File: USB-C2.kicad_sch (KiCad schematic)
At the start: 92 parts, among them J4 USB_C_Receptacle, J5 I2C2_PD_Controller, J6 I2C_Mux, J7 I2C_EEPROM, SW2 FW_Upgrade, U10 24LC256, U11 TPD4E02B04DQA, U12 TPD4E02B04DQA, U13 TPD4E02B04DQA, U14 TUSB1142IRNQR_C5216209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

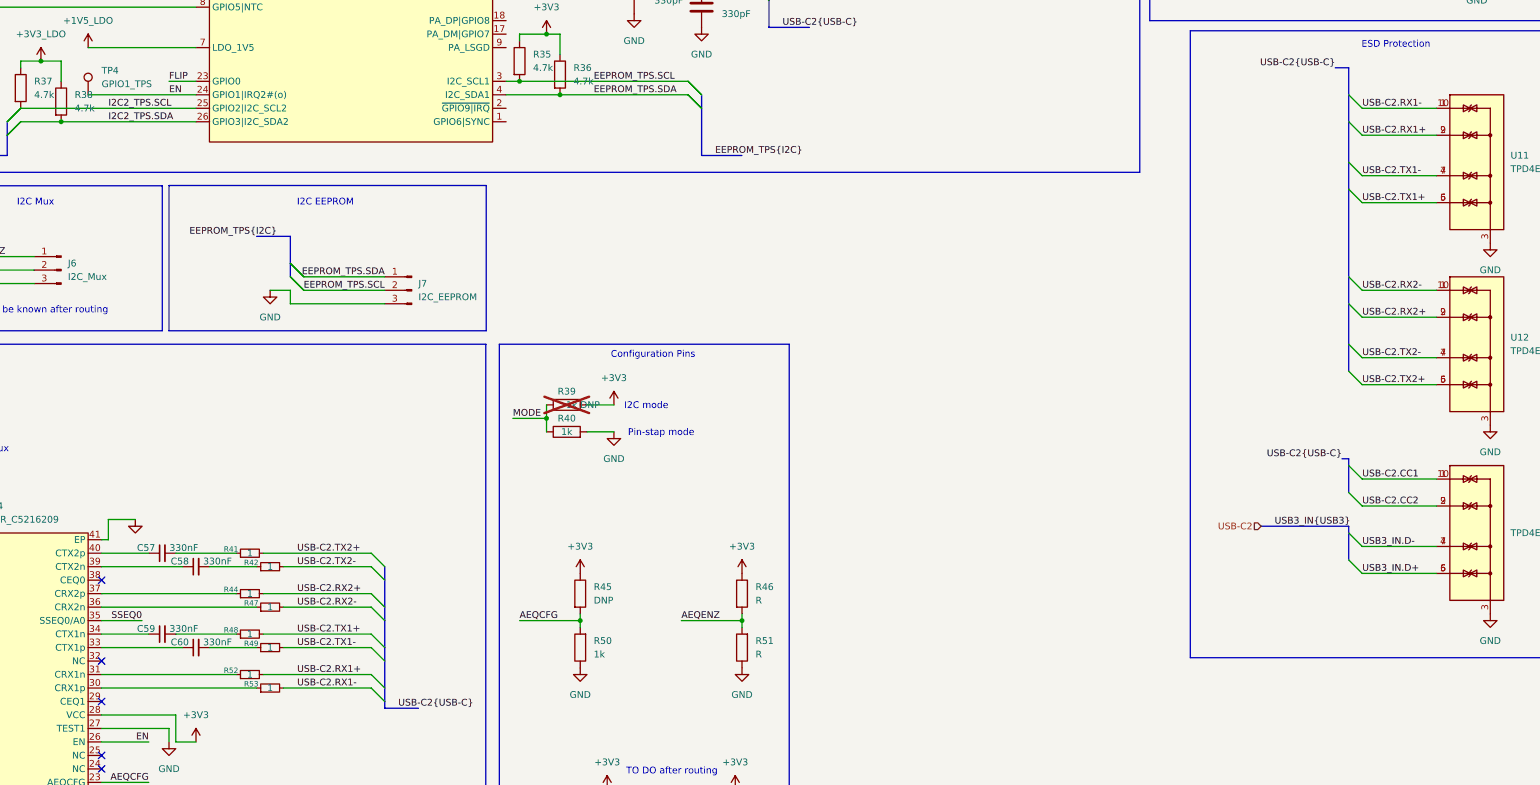
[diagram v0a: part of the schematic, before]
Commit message: Next net class label fixes, swap of the SS lines for better routing
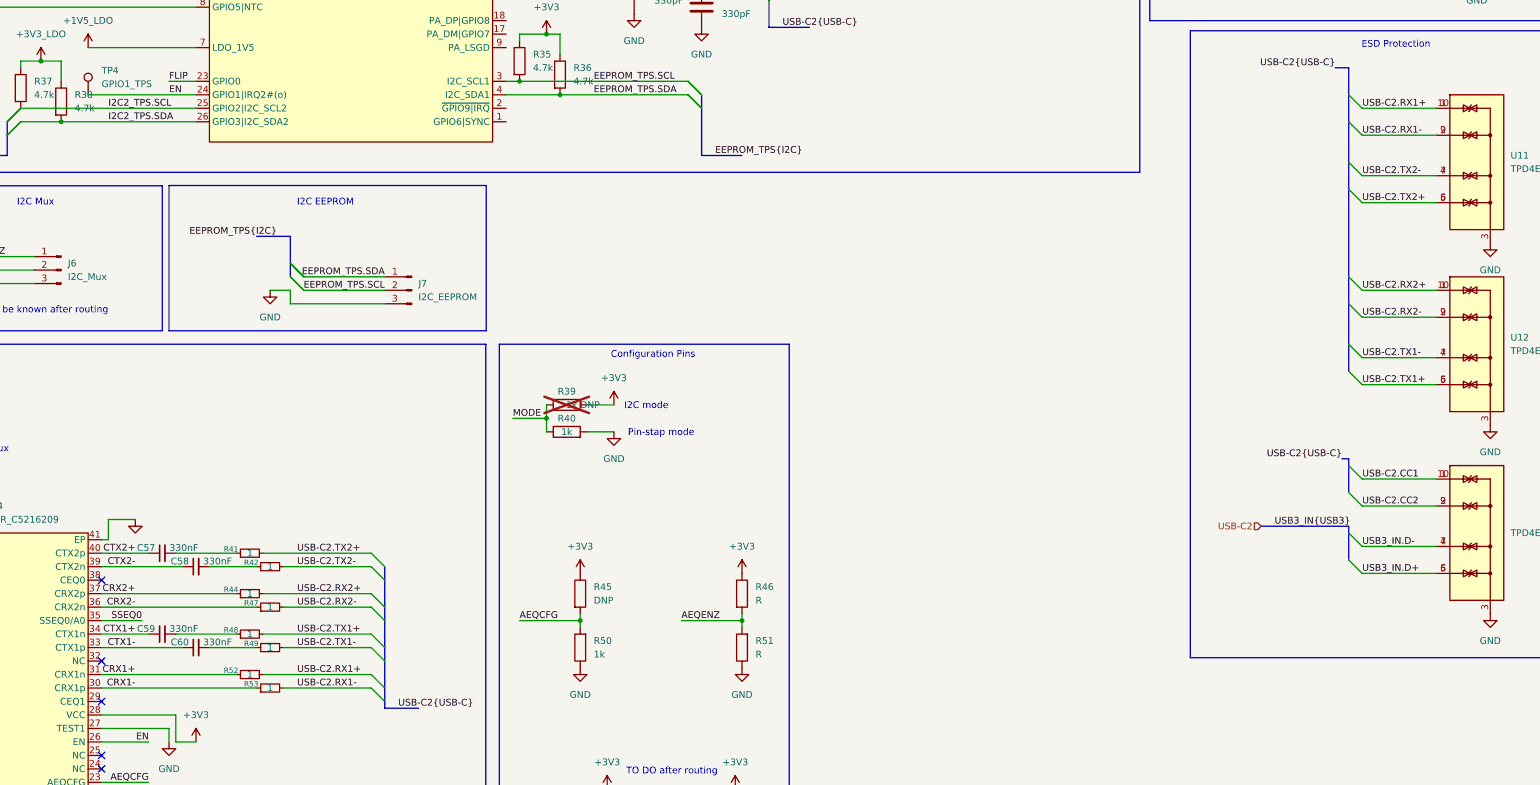
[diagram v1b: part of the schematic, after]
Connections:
- net USB-C2.RX1+: now also U11.1 (IO1), U11.10 (NC); no longer U11.2 (IO2), U11.9 (NC)
- net USB-C2.RX1-: now also U11.2 (IO2), U11.9 (NC); no longer U11.1 (IO1), U11.10 (NC)
- net USB-C2.RX2+: now also U12.1 (IO1), U12.10 (NC); no longer U12.2 (IO2), U12.9 (NC)
- net USB-C2.RX2-: now also U12.2 (IO2), U12.9 (NC); no longer U12.1 (IO1), U12.10 (NC)
- net USB-C2.TX1+: now also U12.5 (IO4), U12.6 (NC); no longer U11.5 (IO4), U11.6 (NC)
- net USB-C2.TX1-: now also U12.4 (IO3), U12.7 (NC); no longer U11.4 (IO3), U11.7 (NC)
- net USB-C2.TX2+: now also U11.5 (IO4), U11.6 (NC); no longer U12.5 (IO4), U12.6 (NC)
- net USB-C2.TX2-: now also U11.4 (IO3), U11.7 (NC); no longer U12.4 (IO3), U12.7 (NC)
- net CTX1+: now reaches C59.1, U14.34 (CTX1n)
- net CRX2-: now reaches R47.1, U14.36 (CRX2n)
- net CRX1-: now reaches R53.1, U14.30 (CRX1p)
- net CRX1+: now reaches R52.1, U14.31 (CRX1n)
- net CTX1-: now reaches C60.1, U14.33 (CTX1p)
- net CRX2+: now reaches R44.1, U14.37 (CRX2p)
- net CTX2-: now reaches C58.1, U14.39 (CTX2n)
- net CTX2+: now reaches C57.1, U14.40 (CTX2p)

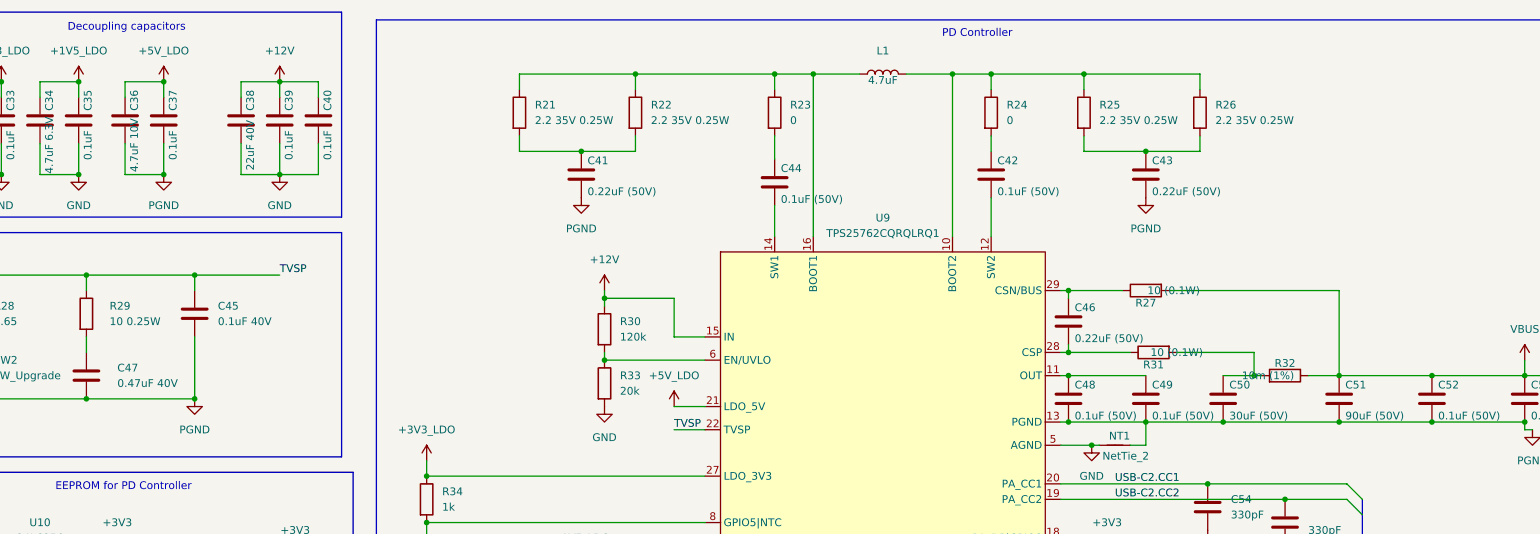
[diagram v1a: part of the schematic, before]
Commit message: Added lcsc part number for most of components, fixes for better routing
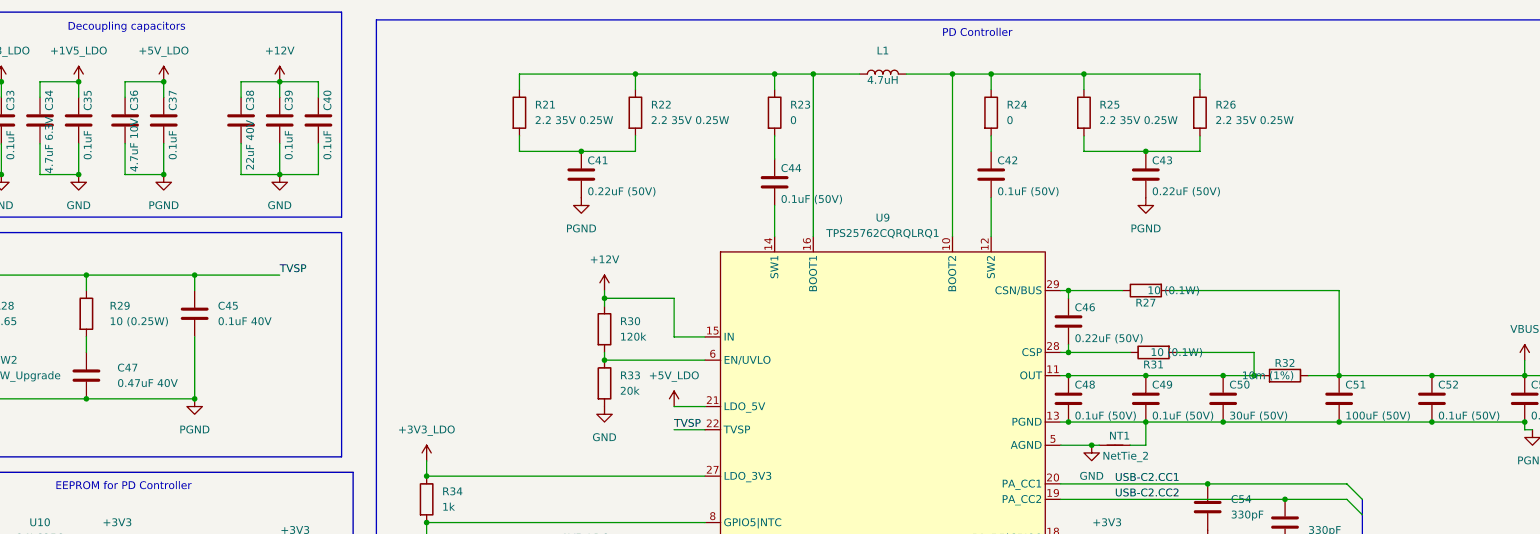
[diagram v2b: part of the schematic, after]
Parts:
- C32, C34, C36: LCSC Part (none) -> C6119944
- C33, C35, C37, C39, C40, C42, C44, C45, C48, C49, C52, C53, C56, C66, C67, C68, C69: LCSC Part (none) -> C5182432
- C38: footprint Capacitor_THT:C_Radial_D10.0mm_H16.0mm_P5.00mm -> Capacitor_THT:C_Radial_D5.0mm_H11.0mm_P2.00mm; LCSC Part (none) -> C88755
- C41, C43, C46, C61, C62, C63, C64: LCSC Part (none) -> C114401
- C47: footprint Capacitor_SMD:C_0402_1005Metric -> Capacitor_SMD:C_0603_1608Metric; LCSC Part (none) -> C513577
- C50: footprint Capacitor_THT:C_Radial_D10.0mm_H16.0mm_P5.00mm -> Capacitor_THT:C_Radial_D5.0mm_H11.0mm_P2.00mm; LCSC Part (none) -> C89792
- C51: value 90uF (50V) -> 100uF (50V); footprint Capacitor_THT:C_Radial_D10.0mm_H16.0mm_P5.00mm -> Capacitor_THT:C_Radial_D6.3mm_H11.0mm_P2.50mm; LCSC Part (none) -> C109392
- C54, C55: LCSC Part (none) -> C325463
- C57, C58, C59, C60: LCSC Part (none) -> C18164591
- C65: footprint Capacitor_THT:C_Radial_D10.0mm_H16.0mm_P5.00mm -> Capacitor_SMD:C_0805_2012Metric; LCSC Part (none) -> C3039694
- L1: value 4.7uF -> 4.7uH; footprint Inductor_SMD:L_6.3x6.3_H3 -> Inductor_SMD:L_Coilcraft_XAL1010-XXX; LCSC Part (none) -> C19271849
- R27: value 10 (0.1W) -> 10 (0.1W); footprint Resistor_SMD:R_0402_1005Metric -> Resistor_SMD:R_0603_1608Metric; LCSC Part (none) -> C510088
- R29: value 10 0.25W -> 10 (0.25W); footprint Resistor_SMD:R_0402_1005Metric -> Resistor_SMD:R_0603_1608Metric; LCSC Part (none) -> C510088
- R31: footprint Resistor_SMD:R_0402_1005Metric -> Resistor_SMD:R_0603_1608Metric; LCSC Part (none) -> C510088
- R32: footprint Resistor_SMD:R_1206_3216Metric -> Resistor_SMD:R_2010_5025Metric; LCSC Part (none) -> C844898
- U11, U12, U13: LCSC Part (none) -> C106794
- U8: LCSC Part (none) -> C523793
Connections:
- net at C50.1, R31.2, R32.2: now also C48.1, C49.1, U9.11 (OUT)

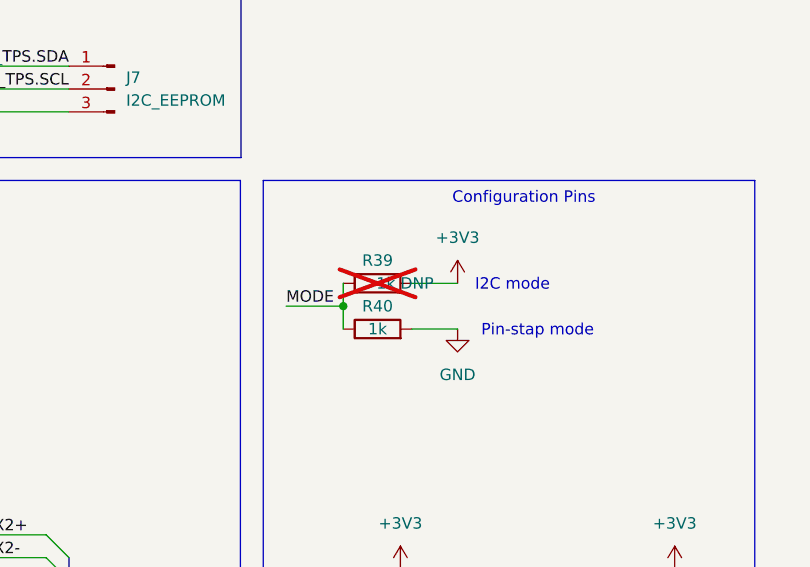
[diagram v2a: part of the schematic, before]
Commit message: Added lcsc part number for most of resistors
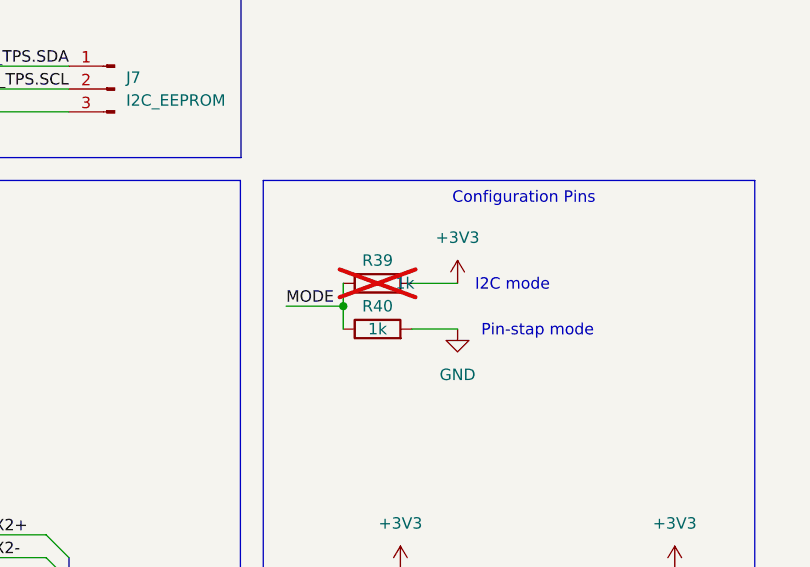
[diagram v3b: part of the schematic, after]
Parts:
- R21, R22, R25, R26: footprint Resistor_SMD:R_0402_1005Metric -> Resistor_SMD:R_0603_1608Metric; LCSC Part (none) -> C966185
- R23, R24: footprint Resistor_SMD:R_0402_1005Metric -> Resistor_SMD:R_0603_1608Metric; LCSC Part (none) -> C2906974
- R28: LCSC Part (none) -> C332644
- R30: LCSC Part (none) -> C93945
- R33: LCSC Part (none) -> C25765
- R34, R40, R43, R50: LCSC Part (none) -> C11702
- R35, R36, R37, R38: LCSC Part (none) -> C105871
- R39: value 1k DNP -> 1k; LCSC Part (none) -> C11702
- R41, R42, R44, R47, R48, R49, R52, R53: LCSC Part (none) -> C185446
